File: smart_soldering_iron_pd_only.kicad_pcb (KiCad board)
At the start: 2 copper layers, 15 x 100 mm, 89 parts, among them J1 Conn_01x04_Pin, J2 TIP_SMALL_END, J3 TIP_MID, U3 ATMEGA328P-AU, U5 CH224K, Y1 16 MHZ

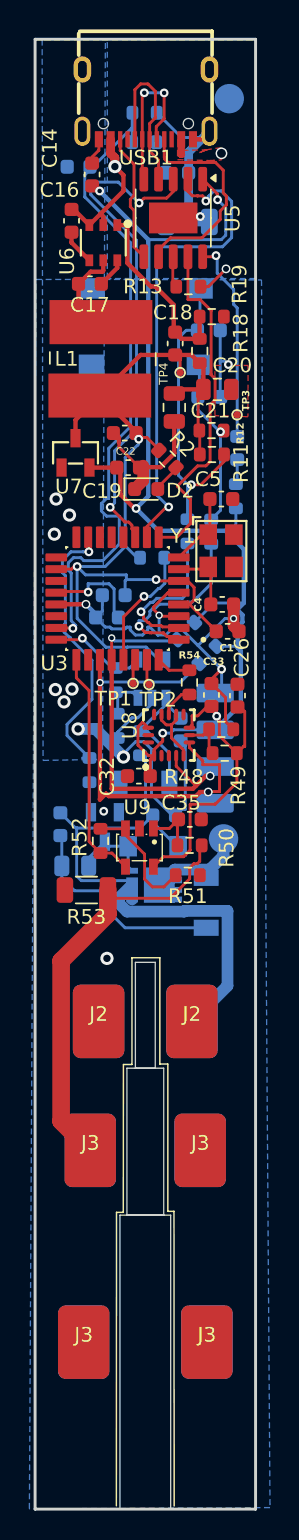
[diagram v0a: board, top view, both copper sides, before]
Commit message: added fillet to the pcb
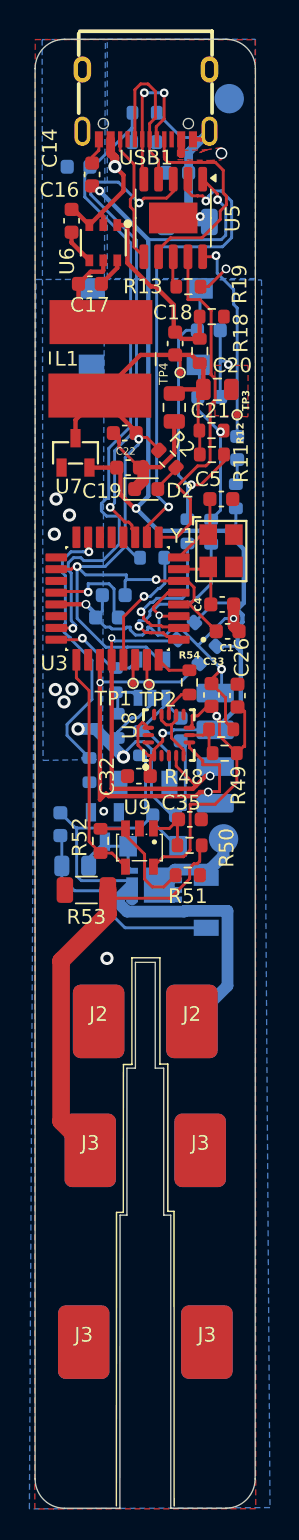
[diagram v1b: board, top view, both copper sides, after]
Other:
- board size 15 x 100 mm -> 15 x 99.9 mm
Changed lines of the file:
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@@
 	)
 	(gr_line
-		(start 193.49 119.72)
-		(end 194.03 119.72)
-		(stroke
-			(width 0.1)
-			(type default)
-		)
-		(layer "F.SilkS")
-	)
-	(gr_line
 		(start 190.53 149.78)
 		(end 190.54 129.81)
@@
 		(layer "F.SilkS")
 	)
-	(gr_rect
-		(start 191.25 120)
-		(end 193.75 130)
+	(gr_line
+		(start 194.03 119.72)
+		(end 193.49 119.72)
+		(stroke
+			(width 0.1)
+			(type default)
+		)
+		(layer "F.SilkS")
+	)
+	(gr_line
+		(start 199.99 52)
+		(end 199.97 147.94)
 		(stroke
 			(width 0.05)
-			(type solid)
+			(type default)
 		)
-		(fill no)
-		(locked yes)
 		(layer "Edge.Cuts")
 	)
-	(gr_rect
-		(start 190.775 130)
-		(end 194.225 150)
+	(gr_line
+		(start 190.77 149.94)
+		(end 190.78 130)
 		(stroke
 			(width 0.05)
-			(type solid)
+			(type default)
 		)
-		(fill no)
-		(locked yes)
 		(layer "Edge.Cuts")
 	)
-	(gr_rect
-		(start 191.825 112.8)
+	(gr_arc
+		(start 185 52)
+		(mid 185.585786 50.585786)
+		(end 187 50)
+		(stroke
+			(width 0.05)
+			(type default)
+		)
+		(layer "Edge.Cuts")
+	)
+	(gr_arc
+		(start 187 149.94)
+		(mid 185.585786 149.354214)
+		(end 185 147.94)
+		(stroke
+			(width 0.05)
+			(type default)
+		)
+		(layer "Edge.Cuts")
+	)
+	(gr_line
+		(start 185 147.94)
+		(end 185 52)
+		(stroke
+			(width 0.05)
+			(type default)
+		)
+		(layer "Edge.Cuts")
+	)
+	(gr_line
+		(start 191.825 120)
+		(end 191.825 112.8)
+		(stroke
+			(width 0.05)
+			(type default)
+		)
+		(layer "Edge.Cuts")
+	)
+	(gr_line
+		(start 187 149.94)
+		(end 190.77 149.94)
+		(stroke
+			(width 0.05)
+			(type default)
+		)
+		(layer "Edge.Cuts")
+	)
+	(gr_line
+		(start 193.175 120)
+		(end 193.75 120)
+		(stroke
+			(width 0.05)
+			(type default)
+		)
+		(layer "Edge.Cuts")
+	)
+	(gr_line
+		(start 197.97 149.94)
+		(end 194.23 149.94)
+		(stroke
+			(width 0.05)
+			(type default)
+		)
+		(layer "Edge.Cuts")
+	)
+	(gr_line
+		(start 193.175 112.8)
 		(end 193.175 120)
 		(stroke
 			(width 0.05)
-			(type solid)
+			(type default)
 		)
-		(fill no)
-		(locked yes)
 		(layer "Edge.Cuts")
 	)
-	(gr_rect
-		(start 185 50)
-		(end 200 150)
+	(gr_line
+		(start 194.23 130)
+		(end 194.23 149.94)
+		(stroke
+			(width 0.05)
+			(type default)
+		)
+		(layer "Edge.Cuts")
+	)
+	(gr_line
+		(start 191.825 112.8)
+		(end 193.175 112.8)
 		(stroke
-			(width 0.2)
-			(type solid)
+			(width 0.05)
+			(type default)
+		)
+		(layer "Edge.Cuts")
+	)
+	(gr_line
+		(start 191.25 120)
+		(end 191.825 120)
+		(stroke
+			(width 0.05)
+			(type default)
+		)
+		(layer "Edge.Cuts")
+	)
+	(gr_line
+		(start 187 50)
+		(end 197.99 50)
+		(stroke
+			(width 0.05)
+			(type default)
+		)
+		(layer "Edge.Cuts")
+	)
+	(gr_line
+		(start 193.75 130)
+		(end 194.23 130)
+		(stroke
+			(width 0.05)
+			(type default)
+		)
+		(layer "Edge.Cuts")
+	)
+	(gr_line
+		(start 190.78 130)
+		(end 191.25 130)
+		(stroke
+			(width 0.05)
+			(type default)
+		)
+		(layer "Edge.Cuts")
+	)
+	(gr_arc
+		(start 199.97 147.94)
+		(mid 199.384214 149.354214)
+		(end 197.97 149.94)
+		(stroke
+			(width 0.05)
+			(type default)
+		)
+		(layer "Edge.Cuts")
+	)
+	(gr_arc
+		(start 197.99 50)
+		(mid 199.404214 50.585786)
+		(end 199.99 52)
+		(stroke
+			(width 0.05)
+			(type default)
+		)
+		(layer "Edge.Cuts")
+	)
+	(gr_line
+		(start 193.75 120)
+		(end 193.75 130)
+		(stroke
+			(width 0.05)
+			(type default)
+		)
+		(layer "Edge.Cuts")
+	)
+	(gr_line
+		(start 191.25 130)
+		(end 191.25 120)
+		(stroke
+			(width 0.05)
+			(type default)
 		)
-		(fill no)
-		(locked yes)
 		(layer "Edge.Cuts")
 	)
@@
 		)
 	)
-	(group ""
-		(locked yes)
-		(members "0ae65965-ea16-41d8-9b04-a1af28c1ac4f" "405898cd-9faf-4880-8f3a-6f68ece2541d"
-			"9f98bd32-295e-4e0f-9339-211dd9803767"
-		)
-	)

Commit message: added reset
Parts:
- added TP7: TestPoint, TestPoint:TestPoint_Pad_D1.5mm, F.Cu at (191.3, 95.2)
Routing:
- net Net-(U3-PC6/~{RESET}): track 8.45 -> 11.6 mm
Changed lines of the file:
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@@
 	(footprint "TestPoint:TestPoint_Pad_D1.5mm"
 		(layer "F.Cu")
+		(at 191.3 95.21)
+		(descr "SMD pad as test Point, diameter 1.5mm")
+		(tags "test point SMD pad")
+		(property "Reference" "TP7"
+			(at 0 -1.648 0)
+			(layer "F.SilkS")
+			(effects
+				(font
+					(size 1 1)
+					(thickness 0.15)
+				)
+			)
+		)
+		(property "Value" "TestPoint"
+			(at 0 1.75 0)
+			(layer "F.Fab")
+			(hide yes)
+			(effects
+				(font
+					(size 1 1)
+					(thickness 0.15)
+				)
+			)
+		)
+		(property "Datasheet" "~"
+			(at 0 0 0)
+			(unlocked yes)
+			(layer "F.Fab")
+			(hide yes)
+			(effects
+				(font
+					(size 1.27 1.27)
+					(thickness 0.15)
+				)
+			)
+		)
+		(property "Description" "test point"
+			(at 0 0 0)
+			(unlocked yes)
+			(layer "F.Fab")
+			(hide yes)
+			(effects
+				(font
+					(size 1.27 1.27)
+					(thickness 0.15)
+				)
+			)
+		)
+		(property ki_fp_filters "Pin* Test*")
+		(sheetname "/")
+		(sheetfile "smart_soldering_iron_pd_only.kicad_sch")
+		(attr exclude_from_pos_files)
+		(fp_circle
+			(center 0.01 0.08)
+			(end 0.34 0.06)
+			(stroke
+				(width 0.12)
+				(type solid)
+			)
+			(fill no)
+			(layer "F.SilkS")
+		)
+		(fp_circle
+			(center 0.01 0.08)
+			(end 0.43 0)
+			(stroke
+				(width 0.05)
+				(type solid)
+			)
+			(fill no)
+			(layer "F.CrtYd")
+		)
+		(pad "1" smd circle
+			(at 0.01 0.08)
+			(size 0.5 0.5)
+			(layers "F.Cu" "F.Mask")
+			(net 62 "Net-(U3-PC6{slash}~{RESET})")
+			(pinfunction "1")
+			(pintype "passive")
+		)
+		(embedded_fonts no)
+	)
+	(footprint "TestPoint:TestPoint_Pad_D1.5mm"
+		(layer "F.Cu")
 		(at 191.66 93.74)
 		(descr "SMD pad as test Point, diameter 1.5mm")
@@
 	)
 	(segment
+		(start 191.01 92.22)
+		(end 191.01 94.99)
+		(width 0.2)
+		(layer "F.Cu")
+		(net 62)
+	)
+	(segment
 		(start 192.41 87.9)
 		(end 191.02 89.29)
@@
 	)
 	(segment
+		(start 191.01 94.99)
+		(end 191.31 95.29)
+		(width 0.2)
+		(layer "F.Cu")
+		(net 62)
+	)
+	(segment
 		(start 191.02 89.29)
 		(end 191.02 92.21)
@@
 		(polygon
 			(pts
-				(xy 189.78164 50.002272) (xy 185.479488 50.022282) (xy 185.541094 99.060641) (xy 189.584587 98.99325)
+				(xy 189.741598 50.002459) (xy 184.990808 50.024555) (xy 185.011394 66.411142) (xy 189.675911 66.333401)
 			)
 		)
@@
 		(polygon
 			(pts
-				(xy 189.71 66.34) (xy 200.403147 66.373243) (xy 200.983085 149.894381) (xy 184.612682 149.982572)
-				(xy 185.06379 66.34)
+				(xy 189.71 66.34) (xy 199.715703 66.371106) (xy 200.295682 149.898084) (xy 184.769335 149.981728)
+				(xy 185.220439 66.34)
 			)
 		)

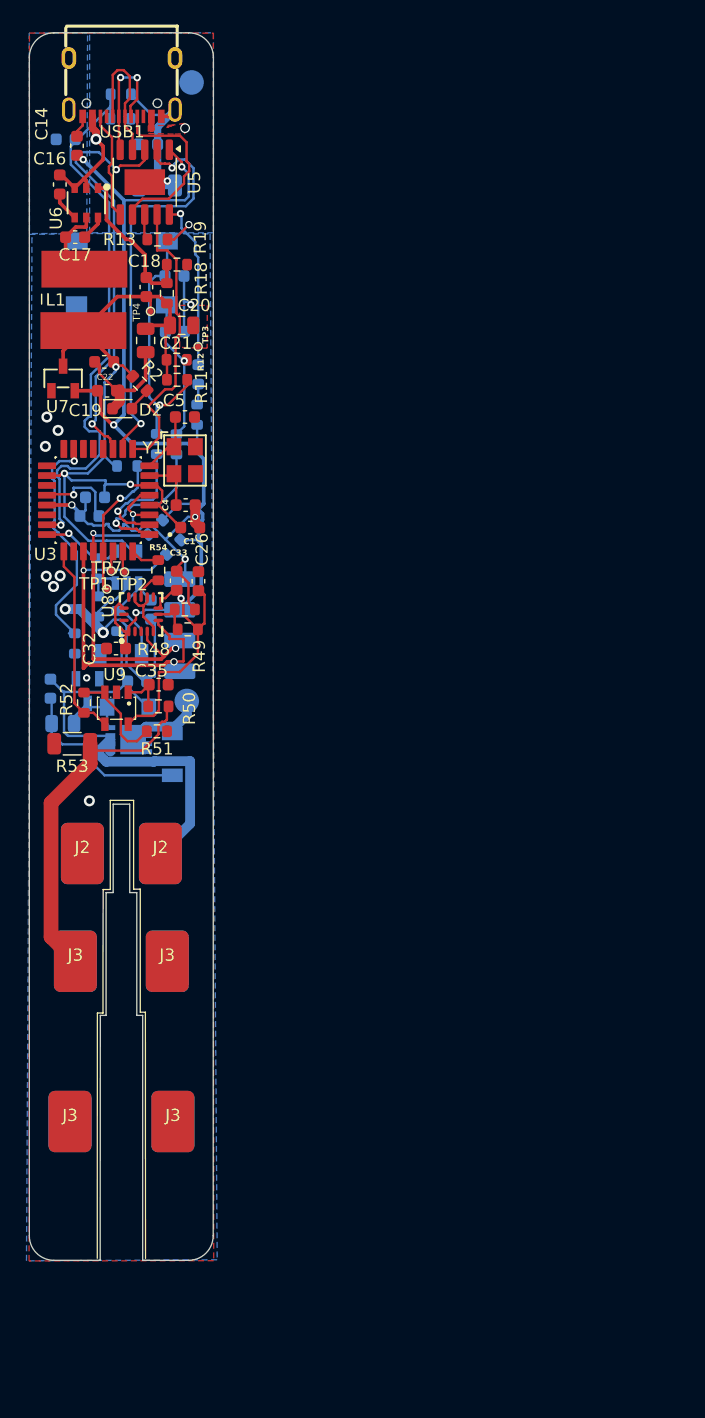
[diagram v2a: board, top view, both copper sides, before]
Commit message: added name and version to the silk screen
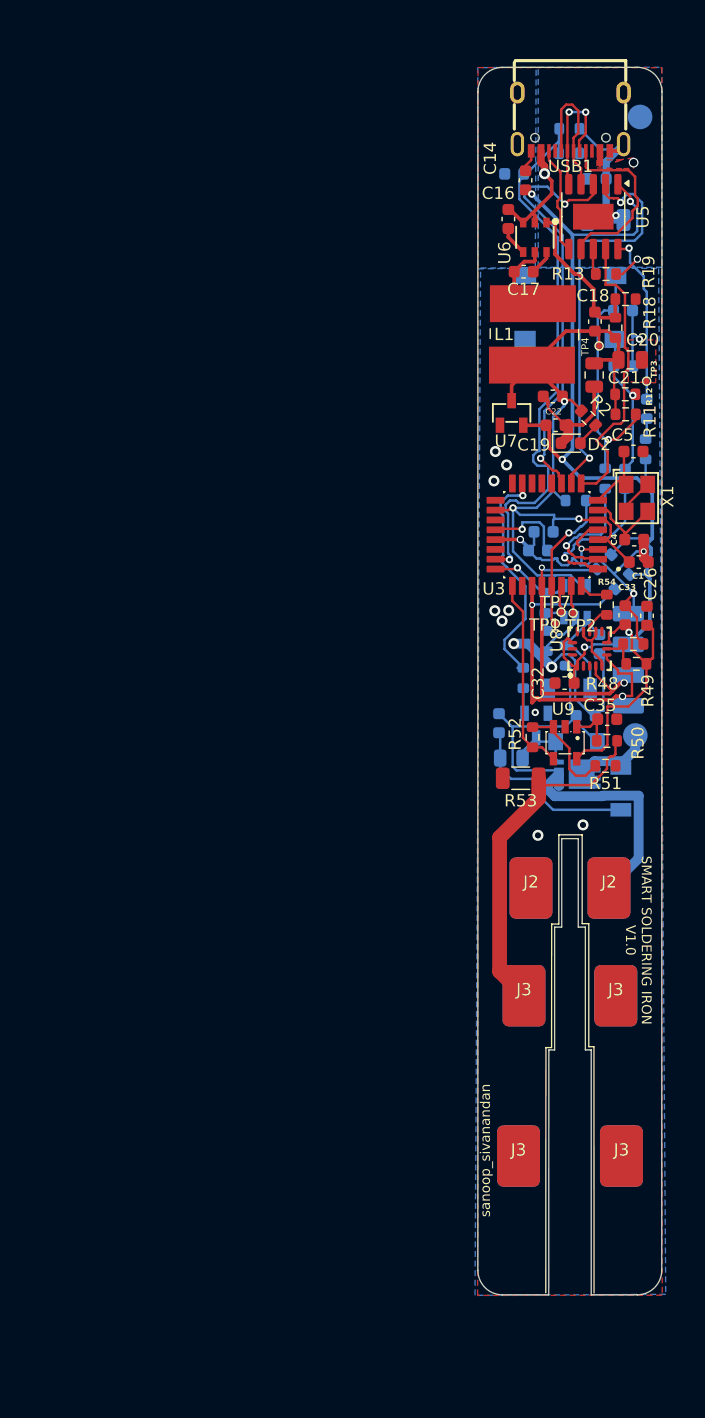
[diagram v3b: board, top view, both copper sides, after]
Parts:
- removed Y1: 16 MHZ, smart_soldering_iron:16_mhz_OSC-SMD_4P-L3.2-W2.5-BL
- added X1: 16MHz, smart_soldering_iron:16_mhz_OSC-SMD_4P-L3.2-W2.5-BL, F.Cu at (234.5, 87.9)
- moved TP1 36.8 mm to (228.3, 97.1)
- moved TP2 36.7 mm to (229.3, 97.2)
- moved C1 36.6 mm to (234.6, 93.1)
- moved C10 36.6 mm to (233.3, 72.6)
- moved C11 36.6 mm to (233.4, 77.1)
- moved C14 36.6 mm to (225.4, 62.0)
- moved C16 36.6 mm to (224.0, 65.2)
- moved C17 36.6 mm to (225.2, 69.5)
- moved C18 36.6 mm to (231.1, 73.5)
- moved C2 36.6 mm to (230.3, 105.6)
- moved C21 36.6 mm to (231.0, 77.9)
- moved C22 36.6 mm to (227.6, 79.6)
- moved C25 36.6 mm to (223.2, 106.2)
- moved C27 36.6 mm to (231.9, 65.2)
- moved C28 36.6 mm to (231.2, 61.9)
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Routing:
- net GND: track 94.1 -> 97.4 mm, vias 16 -> 17
- net XAL1: track 4.69 -> 6.81 mm
- net D0_RXD: track 1.66 -> 2.24 mm
- net D1_TXD: track 1.74 -> 2.28 mm
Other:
- board text added: "SMART SOLDERING IRON V1.0"
- board text added: "sanoop_sivanandan"

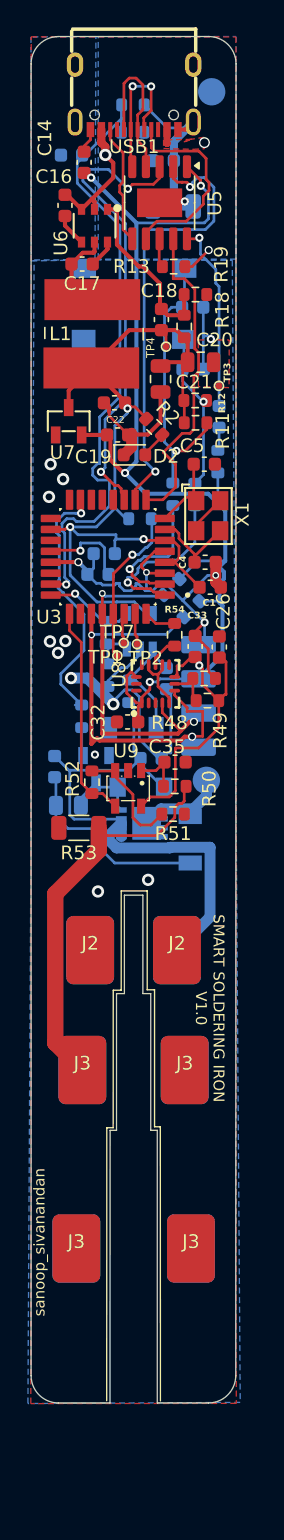
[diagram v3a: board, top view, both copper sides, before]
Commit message: error in tip dimension,added buzzer,increased length to 11cm
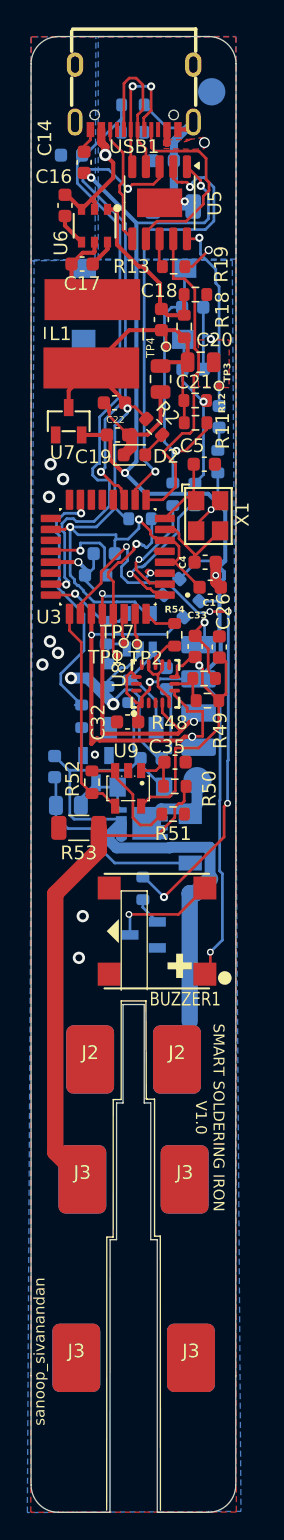
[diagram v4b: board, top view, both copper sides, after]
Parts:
- added BUZZER1: 2.7kHz, smart_soldering_iron:BUZZER_7525A_BUZ-SMD_4P-L7.5-W7.5-P7.59-TL, F.Cu at (230.7, 118.2)
- added Q1: ~, smart_soldering_iron:S8050_TRANSIS_25V_0.5A_npn_SOT-23-3_L2.9-W1.3-P1.90-LS2.4-BR, B.Cu at (229.8, 118.5)
- added R15: 10K, Resistor_SMD:R_0603_1608Metric, B.Cu at (229.7, 115.1)
- moved J3 8.00 mm to (224.8, 149.4) (x2)
- moved J3 8.00 mm to (233.2, 149.4) (x2)
- moved J2 8.00 mm to (232.2, 127.6) (x2)
- moved J2 8.00 mm to (225.8, 127.6) (x2)
- moved J3 8.00 mm to (232.8, 136.4) (x2)
- moved J3 8.00 mm to (225.3, 136.4) (x2)
- moved TP6 0.69 mm to (233.7, 107.2)
- moved C6 0.18 mm to (226.2, 92.2)
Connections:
- U3 pad 26: unconnected-(U3-PC3-Pad26) -> BUZZER
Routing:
- net BUZZER: track 0.00 -> 42.6 mm, vias 0 -> 5
- net VCC_3V3: track 102.9 -> 125.9 mm, vias 5 -> 6
- net GND: track 97.4 -> 81.8 mm, vias 17 -> 18
- net TIP+: track 41.1 -> 49.4 mm
- net TIP-: track 28.9 -> 36.9 mm
- net Net-(BUZZER1--): track 0.00 -> 7.88 mm, vias 0 -> 1
- net Net-(Q1-B): track 0.00 -> 2.07 mm
- net VCC_5V: track 66.9 -> 68.9 mm
- net <_BUTTON: track 10.3 -> 8.52 mm
- net >_BUTTON: track 12.4 -> 10.8 mm
- net Net-(U3-PC6/~{RESET}): track 11.6 -> 12.7 mm
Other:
- board size 15 x 99.9 mm -> 15 x 107.9 mm
